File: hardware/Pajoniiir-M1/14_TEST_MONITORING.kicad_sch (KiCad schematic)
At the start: 12 parts

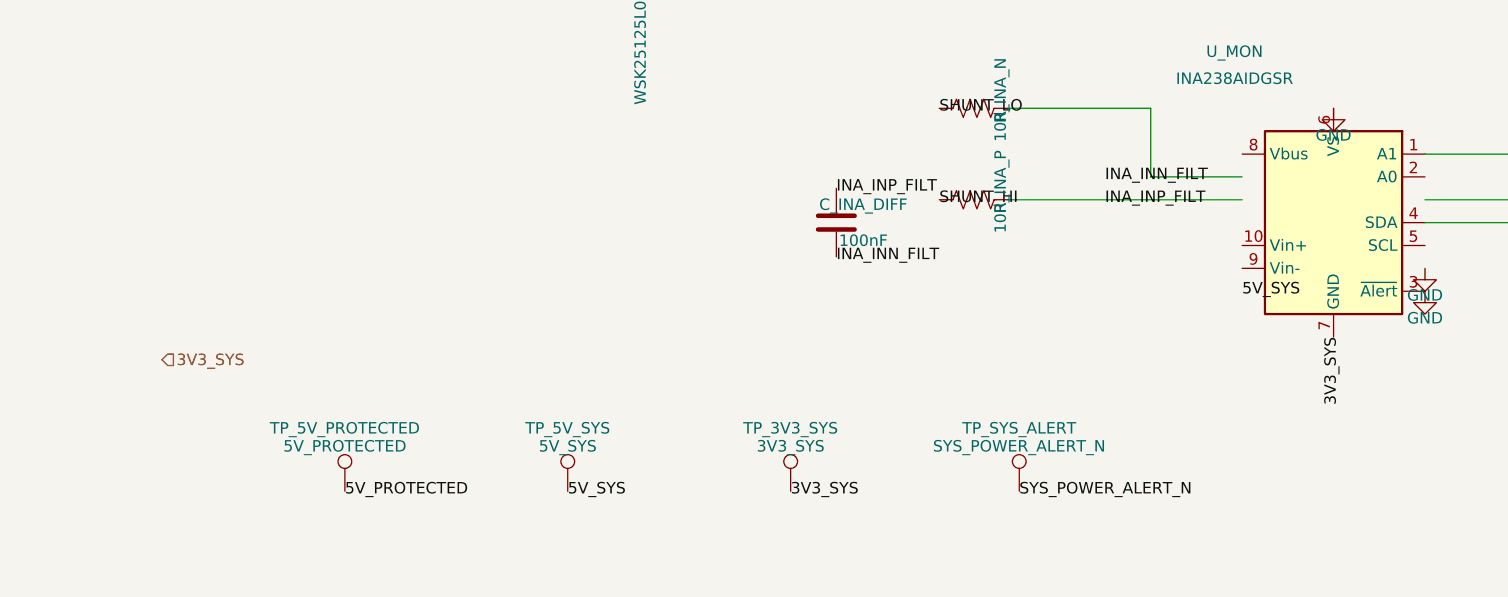
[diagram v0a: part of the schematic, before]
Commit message: hardware: bind remaining hierarchical ports to nets
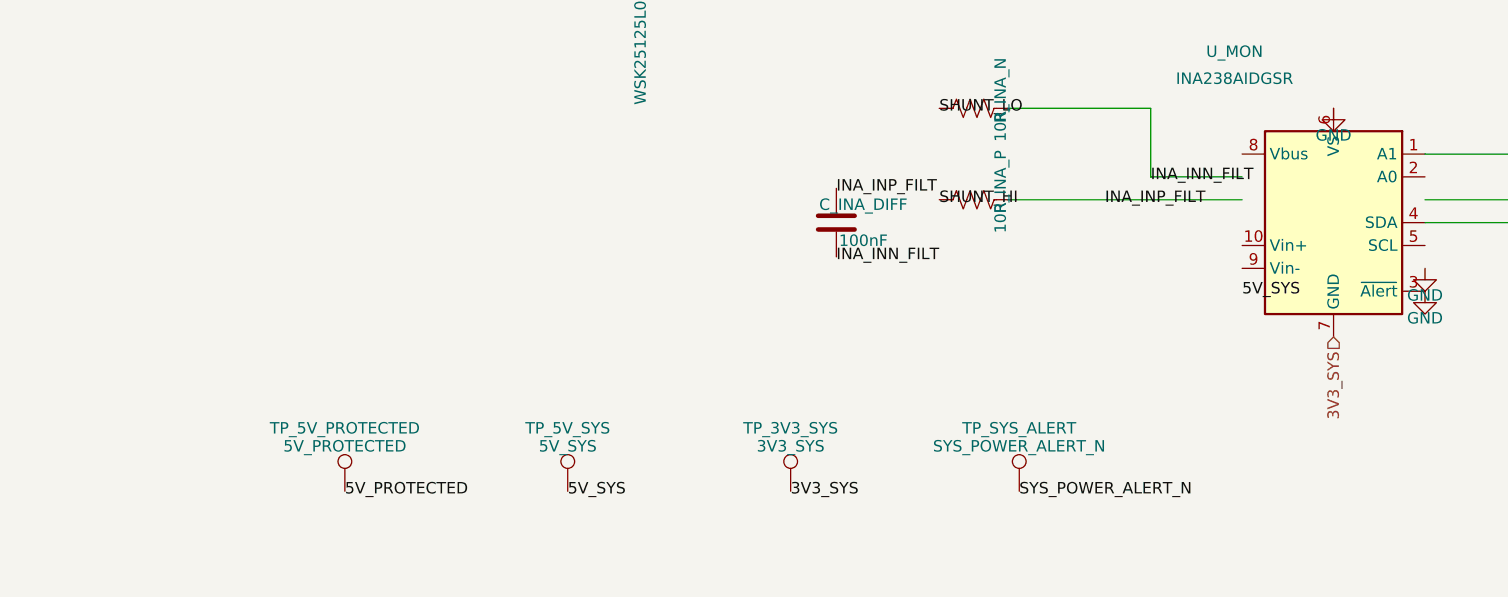
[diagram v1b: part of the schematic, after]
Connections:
- net INA_INN_FILT: now also R_INA_N.2
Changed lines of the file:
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@@
   (wire (pts (xy 144.78 62.23) (xy 144.78 69.85)) (stroke (width 0) (type default)))
   (wire (pts (xy 144.78 69.85) (xy 154.94 69.85)) (stroke (width 0) (type default)))
-  (label "INA_INN_FILT" (at 139.7 69.85 0) (effects (font (size 1.27 1.27))))
+  (label "INA_INN_FILT" (at 144.78 69.85 0) (effects (font (size 1.27 1.27))))
   (symbol
     (lib_id "Device:C") (at 109.855 74.93 0) (unit 1)
@@
   (label "INA_INN_FILT" (at 109.855 78.74 0) (effects (font (size 1.27 1.27))))
   (label "5V_SYS" (at 154.94 82.55 0) (effects (font (size 1.27 1.27))))
-  (hierarchical_label "3V3_SYS" (shape input) (at 34.925 90.17 0) (effects (font (size 1.27 1.27))))
-  (label "3V3_SYS" (at 165.1 87.63 270) (effects (font (size 1.27 1.27))))
+  (hierarchical_label "3V3_SYS" (shape input) (at 165.1 87.63 270) (effects (font (size 1.27 1.27))))
   (symbol
     (lib_id "Device:C") (at 189.865 93.98 0) (unit 1)

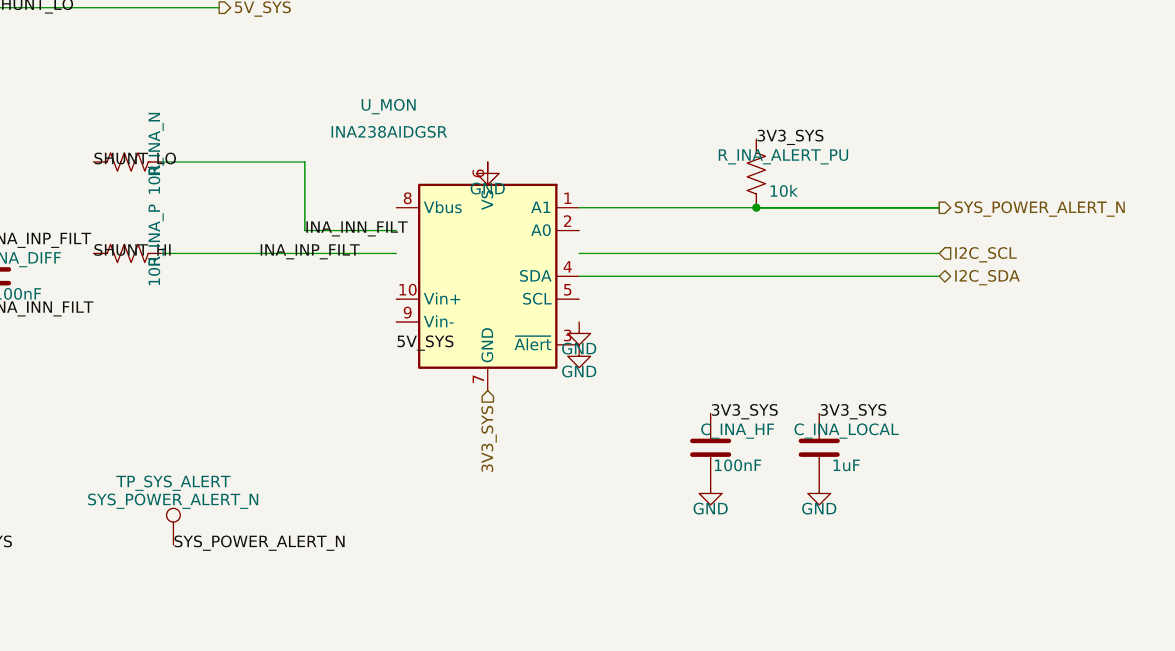
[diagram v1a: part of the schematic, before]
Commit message: hardware: correct INA238 monitor pin mapping
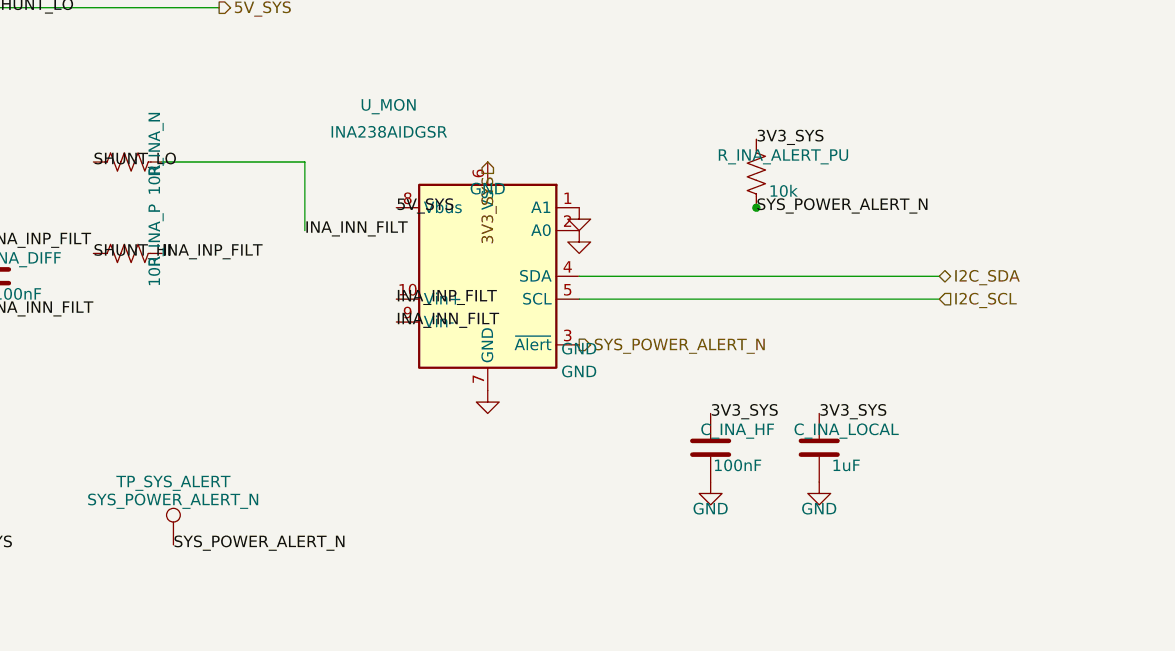
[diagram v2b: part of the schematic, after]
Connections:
- net 3V3_SYS: now also U_MON.6 (VS); no longer U_MON.7 (GND)
- net 5V_SYS: now also U_MON.8 (Vbus)
- net GND: now also U_MON.1 (A1), U_MON.2 (A0), U_MON.7 (GND); no longer U_MON.3 (~{Alert}), U_MON.6 (VS)
- net I2C_SCL: now also U_MON.5 (SCL)
- net INA_INN_FILT: now also U_MON.9 (Vin-)
- net INA_INP_FILT: now also U_MON.10 (Vin+)
- net SYS_POWER_ALERT_N: now also U_MON.3 (~{Alert}); no longer U_MON.1 (A1)
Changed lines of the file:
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@@
     (comment 2 "5mR shunt is in the real power path; monitor IC may be DNP for cost-down")
   )
+  (label "INA_INP_FILT" (at 154.94 77.47 0) (effects (font (size 1.27 1.27))))
+  (label "INA_INN_FILT" (at 154.94 80.01 0) (effects (font (size 1.27 1.27))))
+  (label "SYS_POWER_ALERT_N" (at 194.945 67.31 0) (effects (font (size 1.27 1.27))))
   (junction (at 194.945 67.31) (diameter 0) (color 0 0 0 0))
   (hierarchical_label "5V_PROTECTED" (shape input) (at 34.925 45.085 0) (effects (font (size 1.27 1.27))))
@@
   )
   (label "SHUNT_HI" (at 121.285 72.39 0) (effects (font (size 1.27 1.27))))
-  (wire (pts (xy 128.905 72.39) (xy 154.94 72.39)) (stroke (width 0) (type default)))
-  (label "INA_INP_FILT" (at 139.7 72.39 0) (effects (font (size 1.27 1.27))))
+  (label "INA_INP_FILT" (at 128.905 72.39 0) (effects (font (size 1.27 1.27))))
   (symbol
     (lib_id "Device:R_US") (at 125.095 62.23 90) (unit 1)
@@
   (wire (pts (xy 128.905 62.23) (xy 144.78 62.23)) (stroke (width 0) (type default)))
   (wire (pts (xy 144.78 62.23) (xy 144.78 69.85)) (stroke (width 0) (type default)))
-  (wire (pts (xy 144.78 69.85) (xy 154.94 69.85)) (stroke (width 0) (type default)))
   (label "INA_INN_FILT" (at 144.78 69.85 0) (effects (font (size 1.27 1.27))))
   (symbol
@@
   (label "INA_INP_FILT" (at 109.855 71.12 0) (effects (font (size 1.27 1.27))))
   (label "INA_INN_FILT" (at 109.855 78.74 0) (effects (font (size 1.27 1.27))))
-  (label "5V_SYS" (at 154.94 82.55 0) (effects (font (size 1.27 1.27))))
-  (hierarchical_label "3V3_SYS" (shape input) (at 165.1 87.63 270) (effects (font (size 1.27 1.27))))
+  (label "5V_SYS" (at 154.94 67.31 0) (effects (font (size 1.27 1.27))))
+  (hierarchical_label "3V3_SYS" (shape input) (at 165.1 62.23 270) (effects (font (size 1.27 1.27))))
   (symbol
     (lib_id "Device:C") (at 189.865 93.98 0) (unit 1)
@@
   )
   (symbol
-    (lib_id "power:GND") (at 165.1 62.23 0) (unit 1)
+    (lib_id "power:GND") (at 165.1 87.63 0) (unit 1)
     (exclude_from_sim no) (in_bom yes) (on_board yes) (dnp no)
     (property "Reference" "#PWR1403" (at 165.1 68.23 0) (effects (font (size 1.27 1.27)) (hide yes)))
@@
   )
   (symbol
-    (lib_id "power:GND") (at 175.26 82.55 0) (unit 1)
+    (lib_id "power:GND") (at 175.26 67.31 0) (unit 1)
     (exclude_from_sim no) (in_bom yes) (on_board yes) (dnp no)
     (property "Reference" "#PWR1404" (at 175.26 88.55 0) (effects (font (size 1.27 1.27)) (hide yes)))
@@
   )
   (symbol
-    (lib_id "power:GND") (at 175.26 80.01 0) (unit 1)
+    (lib_id "power:GND") (at 175.26 69.85 0) (unit 1)
     (exclude_from_sim no) (in_bom yes) (on_board yes) (dnp no)
     (property "Reference" "#PWR1405" (at 175.26 86.01 0) (effects (font (size 1.27 1.27)) (hide yes)))
@@
   (hierarchical_label "I2C_SDA" (shape bidirectional) (at 215.265 74.93 0) (effects (font (size 1.27 1.27))))
   (wire (pts (xy 175.26 74.93) (xy 215.265 74.93)) (stroke (width 0) (type default)))
-  (hierarchical_label "I2C_SCL" (shape input) (at 215.265 72.39 0) (effects (font (size 1.27 1.27))))
-  (wire (pts (xy 175.26 72.39) (xy 215.265 72.39)) (stroke (width 0) (type default)))
-  (hierarchical_label "SYS_POWER_ALERT_N" (shape output) (at 215.265 67.31 0) (effects (font (size 1.27 1.27))))
-  (wire (pts (xy 175.26 67.31) (xy 215.265 67.31)) (stroke (width 0) (type default)))
+  (hierarchical_label "I2C_SCL" (shape input) (at 215.265 77.47 0) (effects (font (size 1.27 1.27))))
+  (wire (pts (xy 175.26 77.47) (xy 215.265 77.47)) (stroke (width 0) (type default)))
+  (hierarchical_label "SYS_POWER_ALERT_N" (shape output) (at 175.26 82.55 0) (effects (font (size 1.27 1.27))))
   (symbol
     (lib_id "Device:R_US") (at 194.945 63.5 0) (unit 1)
@@
   )
   (label "3V3_SYS" (at 194.945 59.69 0) (effects (font (size 1.27 1.27))))
-  (wire (pts (xy 194.945 67.31) (xy 215.265 67.31)) (stroke (width 0) (type default)))
   (symbol
     (lib_id "Connector:TestPoint") (at 55.245 104.775 0) (unit 1)

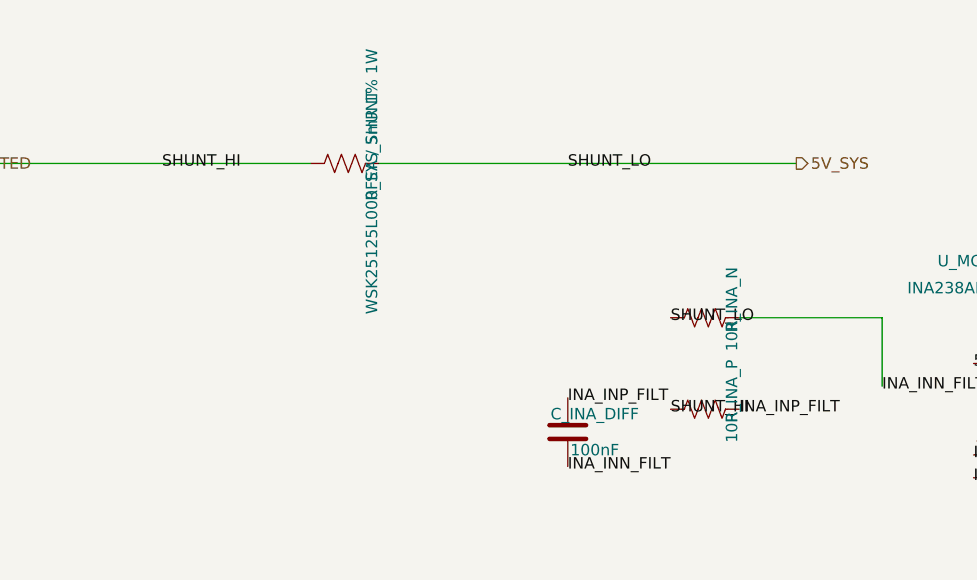
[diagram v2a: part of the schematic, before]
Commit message: hardware: close peripheral endpoint and net-alias gaps
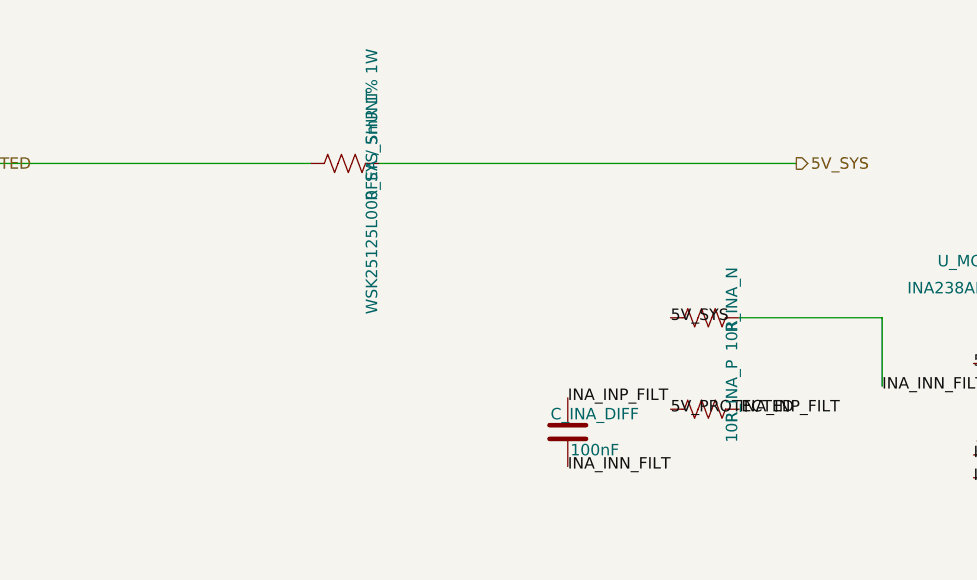
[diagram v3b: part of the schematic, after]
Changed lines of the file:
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@@
   )
   (wire (pts (xy 34.925 45.085) (xy 81.28 45.085)) (stroke (width 0) (type default)))
-  (label "SHUNT_HI" (at 64.77 45.085 0) (effects (font (size 1.27 1.27))))
   (wire (pts (xy 88.9 45.085) (xy 135.255 45.085)) (stroke (width 0) (type default)))
-  (label "SHUNT_LO" (at 109.855 45.085 0) (effects (font (size 1.27 1.27))))
   (hierarchical_label "5V_SYS" (shape output) (at 135.255 45.085 0) (effects (font (size 1.27 1.27))))
   (symbol
@@
     (instances (project "Pajoniiir-M1" (path "/2c8dd352-b7b8-4d9e-8f93-5dd43be2a100/3100000e-6b2a-4a3a-8c91-00000000000e" (reference "R_INA_P") (unit 1))))
   )
-  (label "SHUNT_HI" (at 121.285 72.39 0) (effects (font (size 1.27 1.27))))
+  (label "5V_PROTECTED" (at 121.285 72.39 0) (effects (font (size 1.27 1.27))))
   (label "INA_INP_FILT" (at 128.905 72.39 0) (effects (font (size 1.27 1.27))))
   (symbol
@@
     (instances (project "Pajoniiir-M1" (path "/2c8dd352-b7b8-4d9e-8f93-5dd43be2a100/3100000e-6b2a-4a3a-8c91-00000000000e" (reference "R_INA_N") (unit 1))))
   )
-  (label "SHUNT_LO" (at 121.285 62.23 0) (effects (font (size 1.27 1.27))))
+  (label "5V_SYS" (at 121.285 62.23 0) (effects (font (size 1.27 1.27))))
   (wire (pts (xy 128.905 62.23) (xy 144.78 62.23)) (stroke (width 0) (type default)))
   (wire (pts (xy 144.78 62.23) (xy 144.78 69.85)) (stroke (width 0) (type default)))

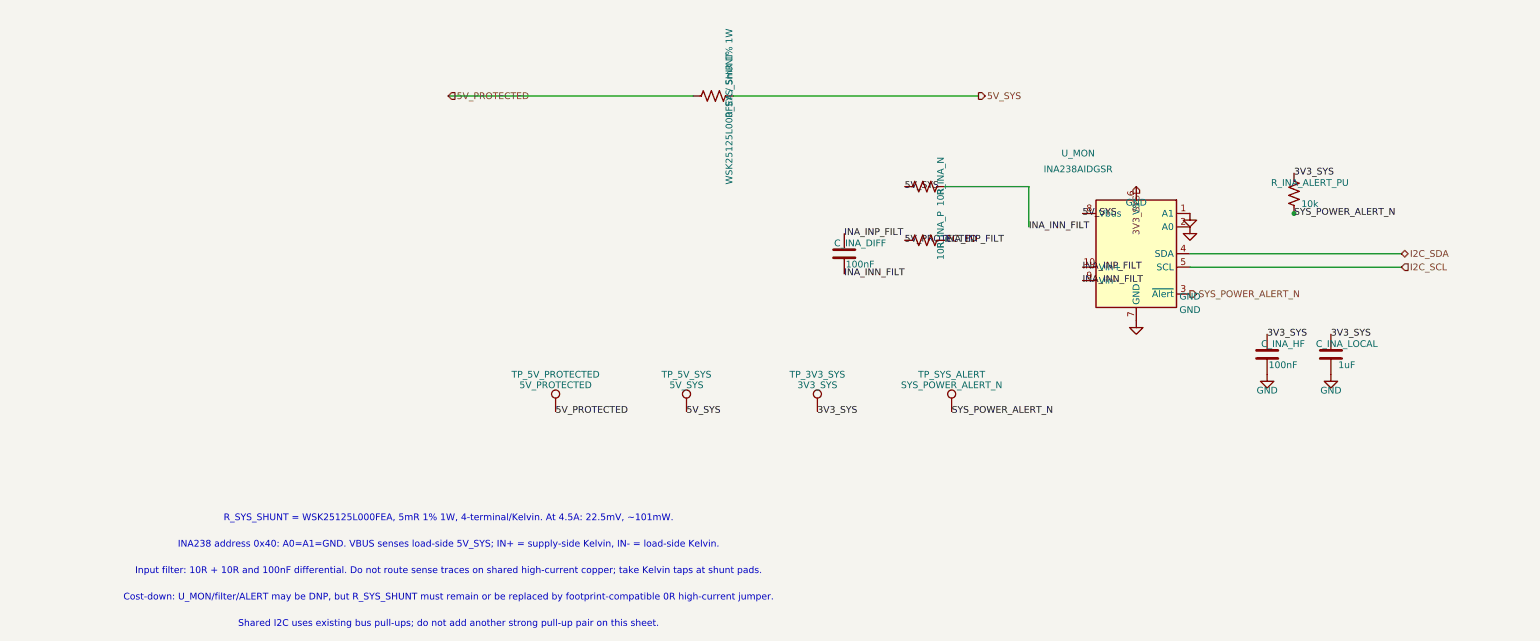
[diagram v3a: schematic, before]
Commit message: hardware: normalize schematic reference designators
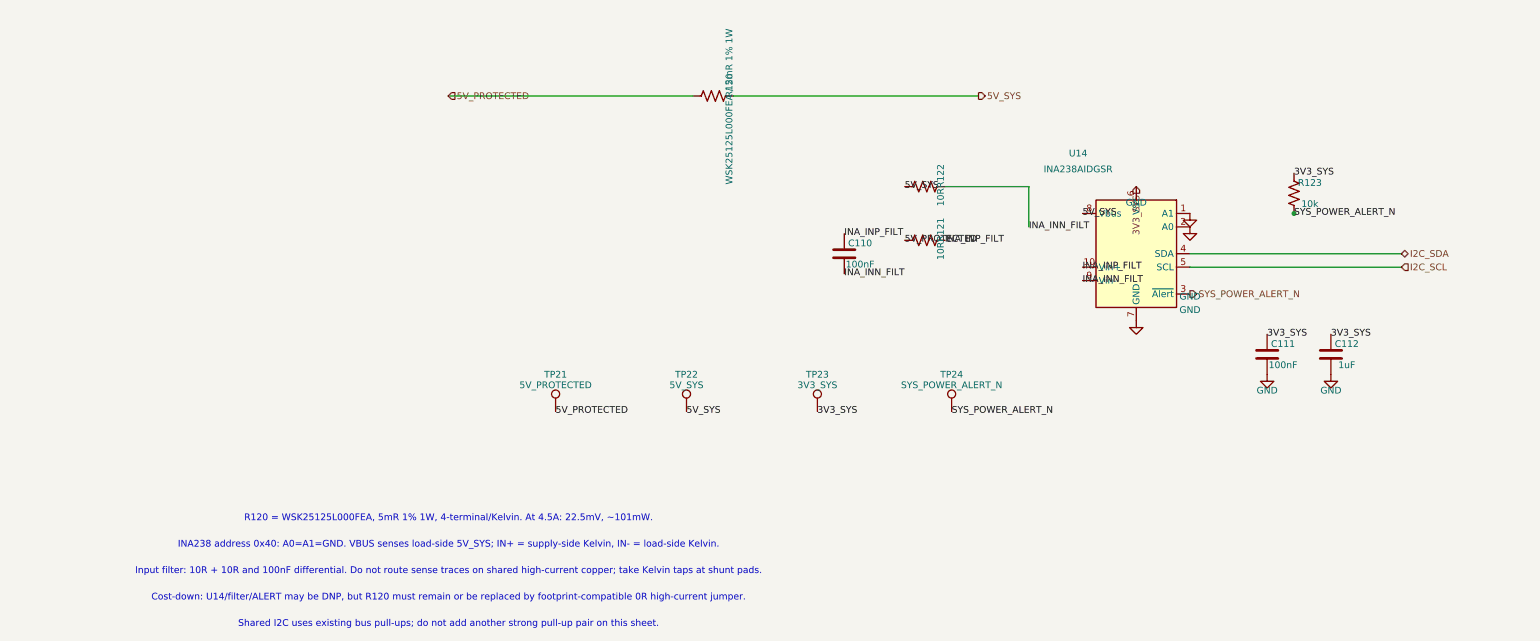
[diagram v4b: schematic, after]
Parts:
- renumbered C_INA_DIFF to C110, C_INA_HF to C111, C_INA_LOCAL to C112, R_SYS_SHUNT to R120, R_INA_P to R121, R_INA_N to R122, R_INA_ALERT_PU to R123, TP_5V_PROTECTED to TP21, TP_5V_SYS to TP22, TP_3V3_SYS to TP23, TP_SYS_ALERT to TP24, U_MON to U14
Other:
- note added: "Cost-down: U14/filter/ALERT may be DNP, but R120 must remain or be replaced by footprint-compatible 0R high-current jumper."
- note added: "R120 = WSK25125L000FEA, 5mR 1% 1W, 4-terminal/Kelvin. At 4.5A: 22.5mV, ~101mW."
- note removed: "Cost-down: U_MON/filter/ALERT may be DNP, but R_SYS_SHUNT must remain or be replaced by footprint-compatible 0R high-current jumper."
- note removed: "R_SYS_SHUNT = WSK25125L000FEA, 5mR 1% 1W, 4-terminal/Kelvin. At 4.5A: 22.5mV, ~101mW."
